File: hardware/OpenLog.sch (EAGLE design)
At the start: 21 parts, among them Q1 16MHZ, U1 ATMEGA328P_TQFP, U2 3.3V MIC5205, U3 microSD Socket

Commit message: Changed c10 to c4
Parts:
- renumbered C10 to C4
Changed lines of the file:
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@@
 </classes>
 <parts>
-<part name="C10" library="SparkFun-Capacitors" deviceset="0.1UF-25V(+80/-20%)(0603)" device="" value="0.1uF"/>
+<part name="C4" library="SparkFun-Capacitors" deviceset="0.1UF-25V(+80/-20%)(0603)" device="" value="0.1uF"/>
 <part name="FRAME1" library="SparkFun-Aesthetics" deviceset="FRAME-LETTER" device=""/>
 <part name="GND25" library="SparkFun" deviceset="GND" device=""/>
@@
 </plain>
 <instances>
-<instance part="C10" gate="G$1" x="48.26" y="139.7"/>
+<instance part="C4" gate="G$1" x="48.26" y="139.7"/>
 <instance part="FRAME1" gate="G$1" x="0" y="0"/>
 <instance part="FRAME1" gate="V" x="147.32" y="0"/>
@@
 <segment>
 <wire x1="48.26" y1="134.62" x2="48.26" y2="137.16" width="0.1524" layer="91"/>
-<pinref part="C10" gate="G$1" pin="2"/>
+<pinref part="C4" gate="G$1" pin="2"/>
 <pinref part="GND26" gate="1" pin="GND"/>
 </segment>
@@
 <pinref part="U2" gate="G$1" pin="OUT"/>
 <pinref part="P+12" gate="G$1" pin="3.3V"/>
-<pinref part="C10" gate="G$1" pin="1"/>
+<pinref part="C4" gate="G$1" pin="1"/>
 <pinref part="C1" gate="G$1" pin="1"/>
 <pinref part="TP1" gate="G$1" pin="1"/>

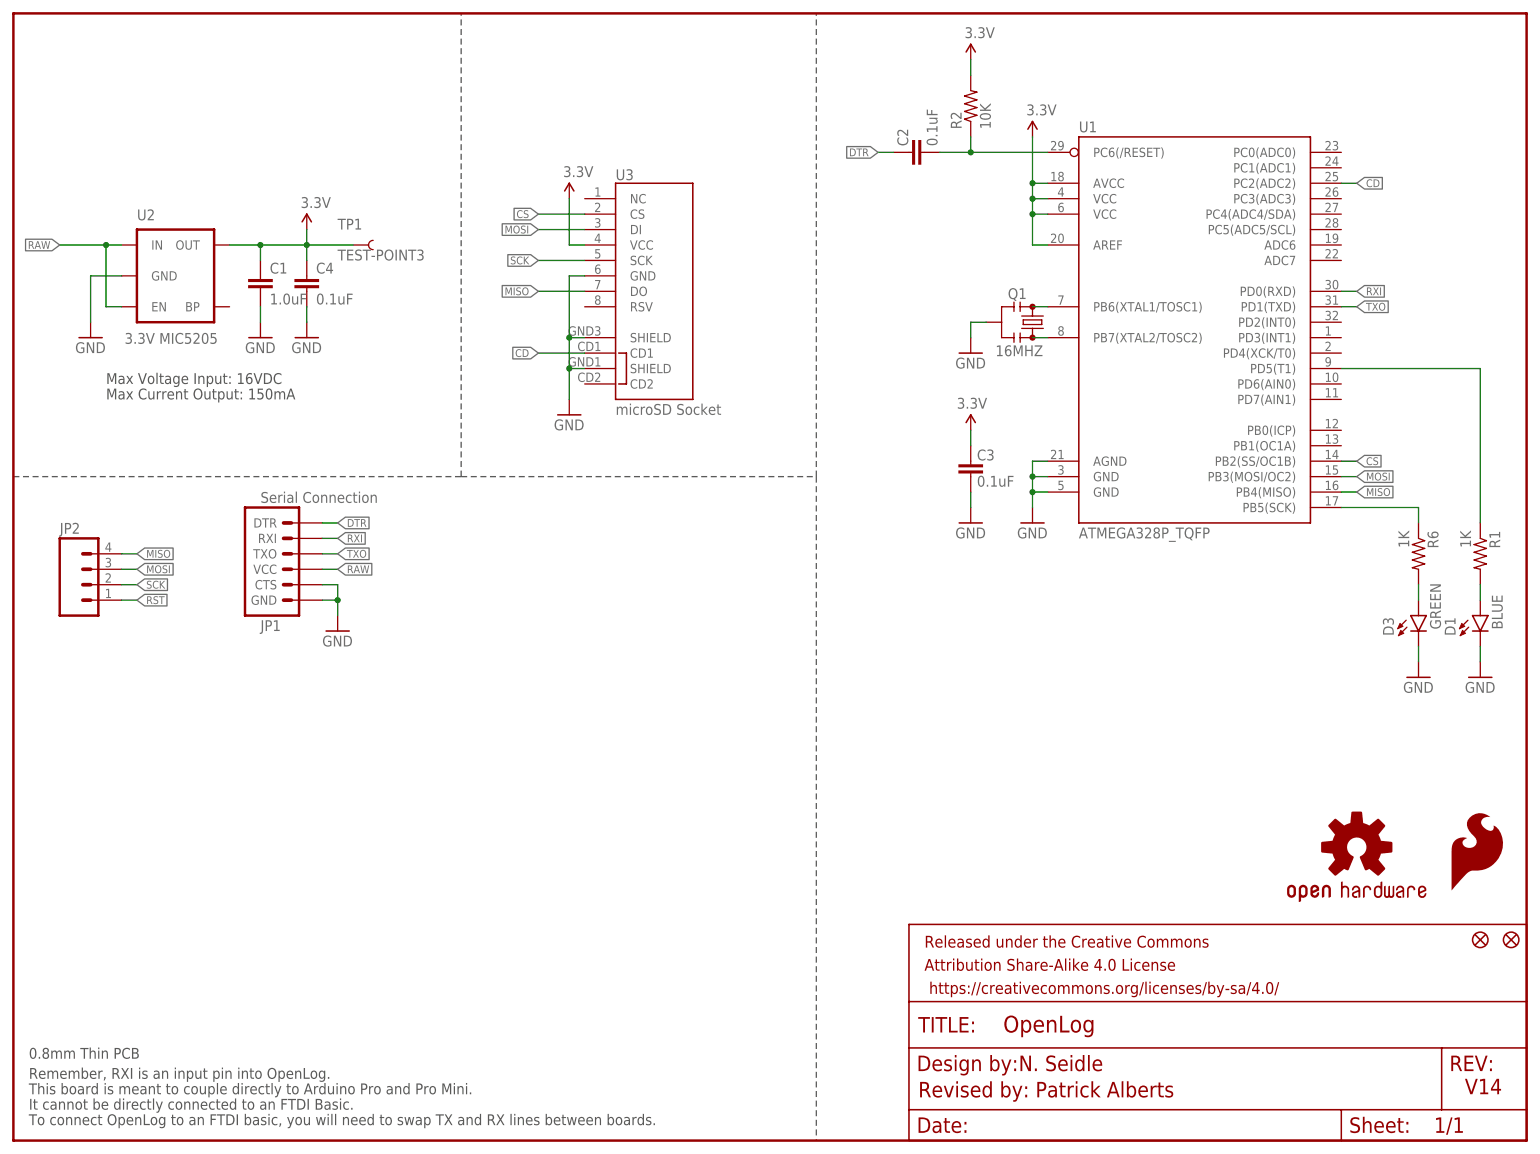
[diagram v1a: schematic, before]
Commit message: Schematic cleanup
Fixed four-way junction and better defined sections of sch.
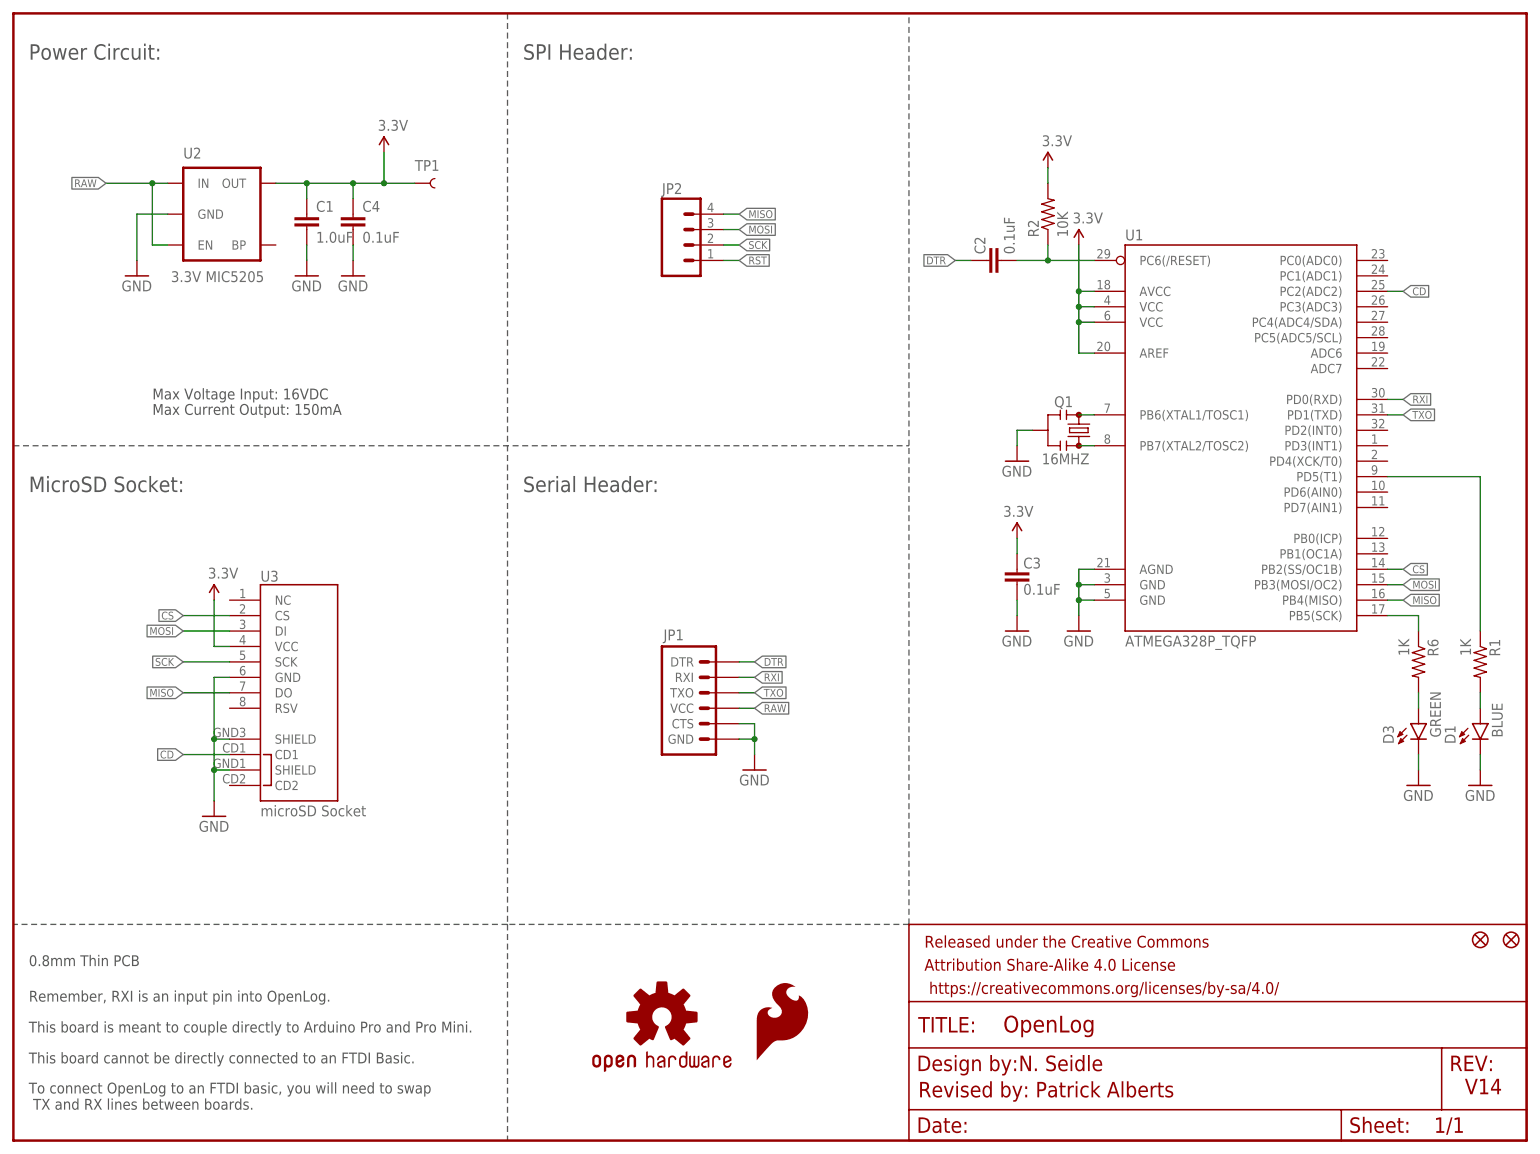
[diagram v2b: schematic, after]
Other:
- note added: "MicroSD Socket:"
- note added: "Power Circuit:"
- note added: "SPI Header:"
- note added: "Serial Header:"
- note added: "This board cannot be directly connected to an FTDI Basic."
- note removed: "It cannot be directly connected to an FTDI Basic."
- moved on the sheet: C1, C2, C3, C4, D1, D3, JP1, JP2, Q1, R1, R2, R6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

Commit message: Adding fiducials to bottom side
Adding fiducials to bottom side for SD card socket placement.
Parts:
- added FID3, FID4: FIDUCIALUFIDUCIAL, SparkFun-Aesthetics:FIDUCIALUFIDUCIAL
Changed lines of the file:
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@@
 <part name="TP1" library="SparkFun-Passives" deviceset="TEST-POINT" device="3"/>
 <part name="LOGO2" library="SparkFun-Aesthetics" deviceset="OSHW-LOGO" device="S"/>
+<part name="FID3" library="SparkFun-Aesthetics" deviceset="FIDUCIAL" device="UFIDUCIAL"/>
+<part name="FID4" library="SparkFun-Aesthetics" deviceset="FIDUCIAL" device="UFIDUCIAL"/>
 </parts>
 <sheets>
@@
 </instance>
 <instance part="LOGO2" gate="G$1" x="106.68" y="20.32"/>
+<instance part="FID3" gate="G$1" x="246.38" y="27.94"/>
+<instance part="FID4" gate="G$1" x="241.3" y="27.94"/>
 </instances>
 <busses>
